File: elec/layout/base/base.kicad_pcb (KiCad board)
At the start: 2 copper layers, 35 parts, among them U1 ?, U2 ?, U3 ?, U4 ?, U5 ?, U6 ?, U7 ?, U8 ?

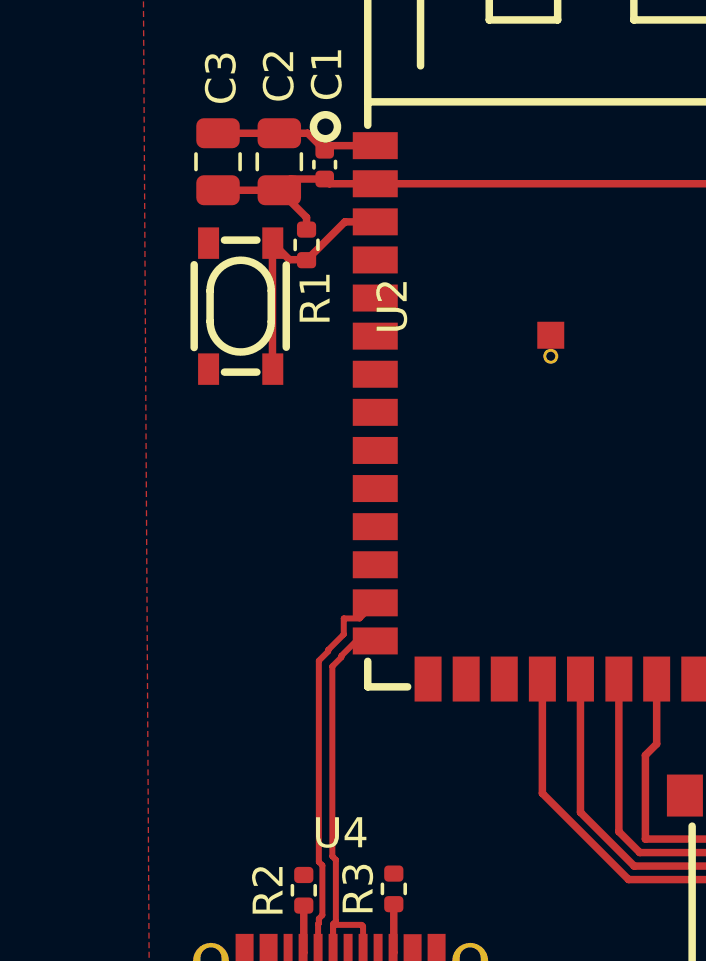
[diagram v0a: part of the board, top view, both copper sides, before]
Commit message: Add connector for display
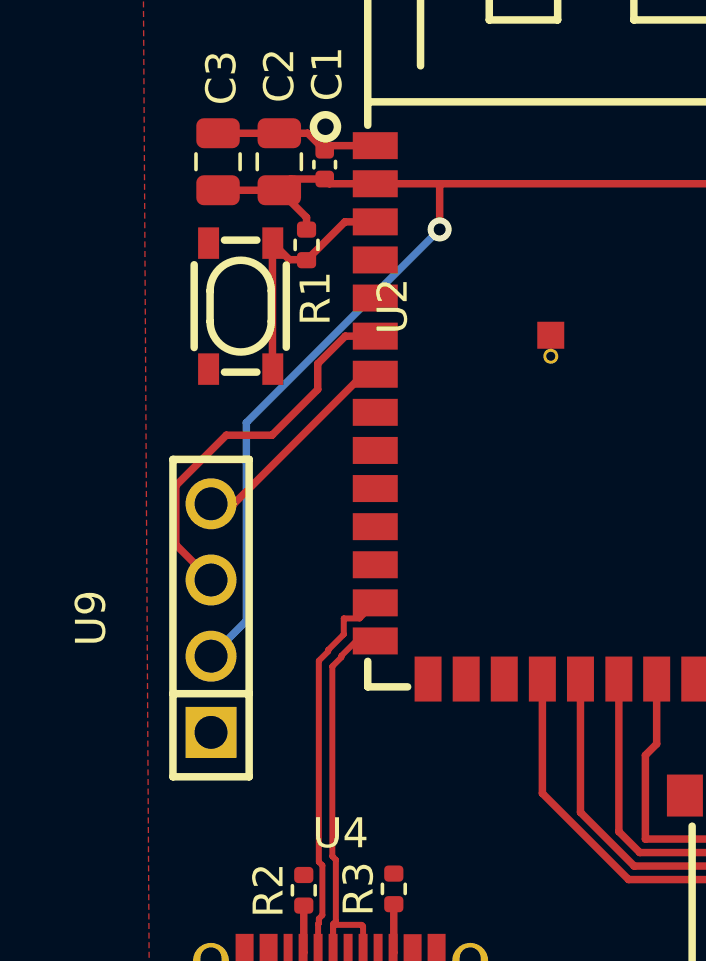
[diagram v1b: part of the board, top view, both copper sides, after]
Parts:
- added U9: ?, lib:HDR-TH_4P-P2.54-V-F, F.Cu at (96.5, 85.3)
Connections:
- U1 pad 6: io6 -> scl
- U1 pad 7: io7 -> sda
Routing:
- net uc.ic-vcc: track 68.0 -> 86.9 mm, vias 2 -> 3
- net scl: track 0.00 -> 12.8 mm
- net sda: track 0.00 -> 7.26 mm

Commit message: Fix and sync layout
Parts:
- added R11: 100mW Thick Film Resistors 75V ±100ppm/℃ ±1% 2.7kΩ 0603 Chi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, lib:R0603, F.Cu at (183.1, 135.6)
- added R12: 100mW Thick Film Resistors 75V ±100ppm/℃ ±1% 2.7kΩ 0603 Chi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, lib:R0603, F.Cu at (183.1, 138.7)
- moved C2 99.7 mm to (183.5, 122.8)
- moved R1 99.7 mm to (184.4, 125.6)
- moved R4 99.7 mm to (214.1, 122.0)
- moved U2 99.7 mm to (182.2, 127.6)
- moved C12 99.7 mm to (215.0, 132.6)
- moved C14 99.7 mm to (208.0, 125.0)
- moved C3 99.7 mm to (181.4, 122.8)
- moved C4 99.7 mm to (213.5, 116.3)
- moved C5 99.7 mm to (213.5, 114.3)
- moved C6 99.7 mm to (213.4, 123.5)
- moved C9 99.7 mm to (214.9, 141.8)
- moved L1 99.7 mm to (217.7, 119.6)
- moved L2 99.7 mm to (210.7, 138.6)
- moved LED1 99.7 mm to (208.9, 135.2)
- moved R10 99.7 mm to (206.9, 135.7)
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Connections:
- net _led.ic-vcc renamed led_dout
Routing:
- net uc.ic-vcc: track 86.9 -> 91.0 mm, vias 3 -> 2
- net uc.ic-gnd: track 31.3 -> 28.1 mm, vias 4 -> 2
- net scl: track 12.8 -> 15.3 mm
- net sda: track 7.26 -> 9.46 mm
- removed copper zone on F.Cu, net uc.ic-gnd
